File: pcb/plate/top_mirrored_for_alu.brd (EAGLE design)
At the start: 109 x 96 mm, 27 parts

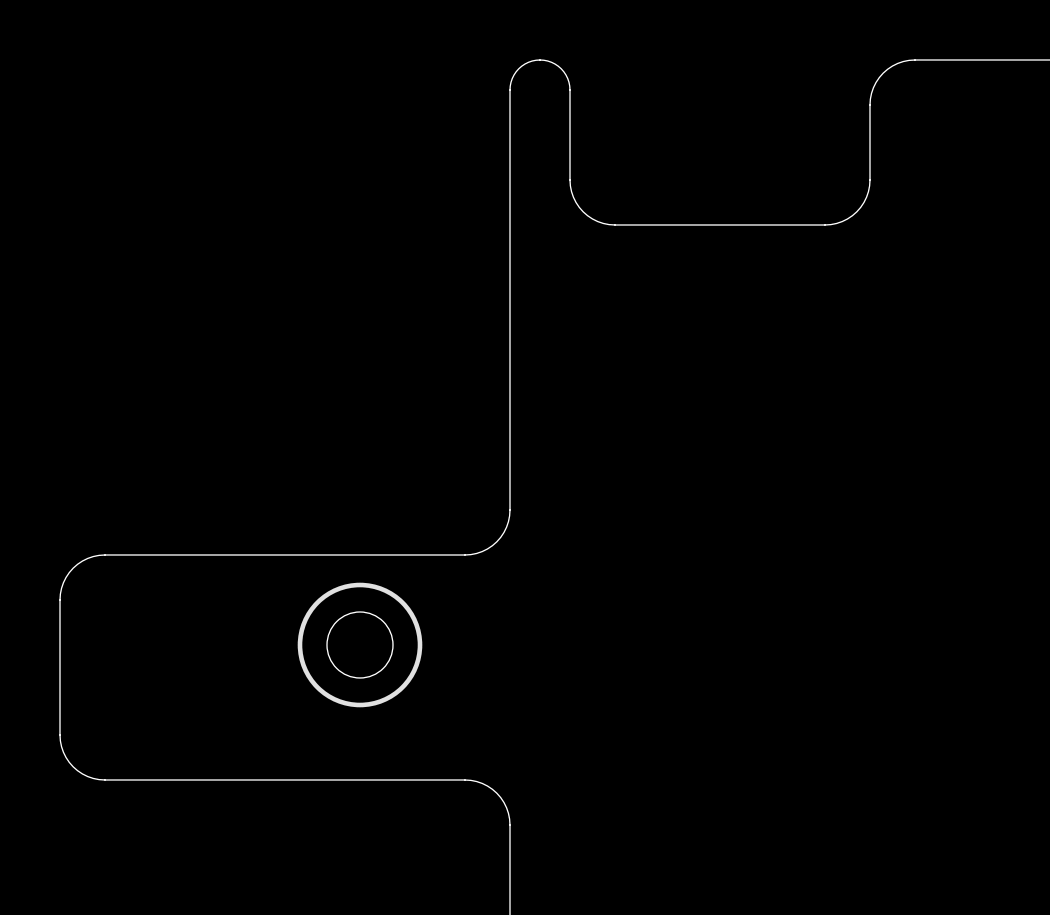
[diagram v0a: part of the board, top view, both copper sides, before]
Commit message: adjusted top plate cutout, removed unused screw hole
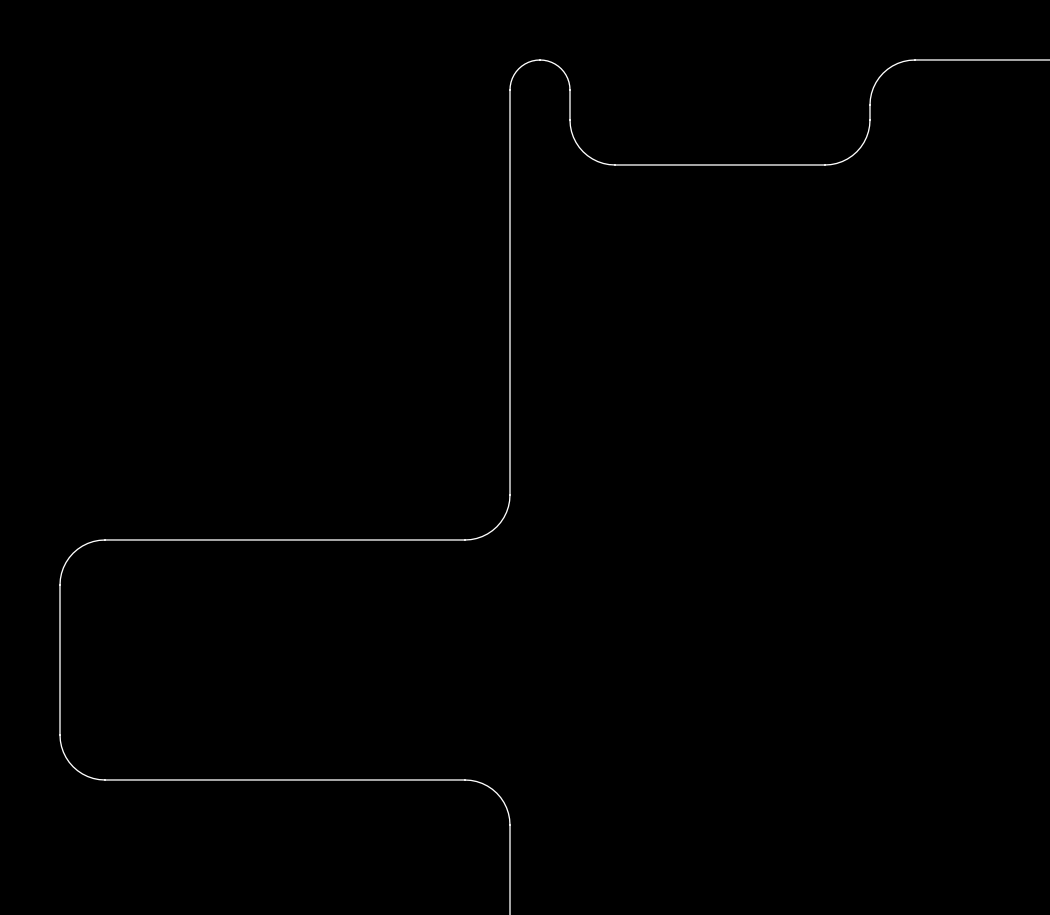
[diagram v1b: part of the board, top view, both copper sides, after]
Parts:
- removed U$17: M2_SCREW_DEV, duckypad:M2_SCREW_FOOT
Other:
- outline, holes or cut-outs redrawn
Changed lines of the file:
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@@
 <wire x1="78.5" y1="96" x2="1.5" y2="96" width="0" layer="20"/>
 <wire x1="1.5" y1="96" x2="0" y2="94.5" width="0" layer="20" curve="90"/>
-<wire x1="0" y1="94.5" x2="0" y2="92" width="0" layer="20"/>
-<wire x1="0" y1="92" x2="-1.5" y2="90.5" width="0" layer="20" curve="-90"/>
-<wire x1="-1.5" y1="90.5" x2="-8.5" y2="90.5" width="0" layer="20"/>
-<wire x1="-8.5" y1="90.5" x2="-10" y2="92" width="0" layer="20" curve="-90"/>
-<wire x1="-10" y1="92" x2="-10" y2="95" width="0" layer="20"/>
+<wire x1="0" y1="94.5" x2="0" y2="94" width="0" layer="20"/>
+<wire x1="0" y1="94" x2="-1.5" y2="92.5" width="0" layer="20" curve="-90"/>
+<wire x1="-1.5" y1="92.5" x2="-8.5" y2="92.5" width="0" layer="20"/>
+<wire x1="-8.5" y1="92.5" x2="-10" y2="94" width="0" layer="20" curve="-90"/>
+<wire x1="-10" y1="94" x2="-10" y2="95" width="0" layer="20"/>
 <wire x1="9.5" y1="0" x2="78.5" y2="0" width="0" layer="20"/>
 <wire x1="78.5" y1="0" x2="82" y2="3.5" width="0" layer="20" curve="90"/>
@@
 <wire x1="6" y1="53" x2="6" y2="3.5" width="0" layer="20"/>
 <wire x1="6" y1="3.5" x2="9.5" y2="0" width="0" layer="20" curve="90"/>
-<wire x1="-13.5" y1="79.5" x2="-25.5" y2="79.5" width="0" layer="20"/>
-<wire x1="-25.5" y1="79.5" x2="-27" y2="78" width="0" layer="20" curve="90"/>
-<wire x1="-27" y1="78" x2="-27" y2="73.5" width="0" layer="20"/>
+<wire x1="-12" y1="95" x2="-12" y2="81.5" width="0" layer="20"/>
+<wire x1="-12" y1="81.5" x2="-13.5" y2="80" width="0" layer="20" curve="-90"/>
+<wire x1="-13.5" y1="80" x2="-25.5" y2="80" width="0" layer="20"/>
+<wire x1="-25.5" y1="80" x2="-27" y2="78.5" width="0" layer="20" curve="90"/>
+<wire x1="-27" y1="78.5" x2="-27" y2="73.5" width="0" layer="20"/>
 <wire x1="-27" y1="73.5" x2="-25.5" y2="72" width="0" layer="20" curve="90"/>
 <wire x1="-25.5" y1="72" x2="-13.5" y2="72" width="0" layer="20"/>
@@
 <wire x1="-10" y1="95" x2="-11" y2="96" width="0" layer="20" curve="90"/>
 <wire x1="-11" y1="96" x2="-12" y2="95" width="0" layer="20" curve="90"/>
-<wire x1="-12" y1="95" x2="-12" y2="81" width="0" layer="20"/>
-<wire x1="-12" y1="81" x2="-13.5" y2="79.5" width="0" layer="20" curve="-90"/>
 <text x="157" y="50" size="1.778" layer="51">big round corner 3.5mm</text>
 </plain>
@@
 <element name="U$12" library="duckypad" package="M2_SCREW_FOOT" value="M2_SCREW_DEV" x="43.5" y="38.5" smashed="yes" rot="MR0"/>
 <element name="U$13" library="duckypad" package="M2_SCREW_FOOT" value="M2_SCREW_DEV" x="24.5" y="19.5" smashed="yes" rot="MR0"/>
-<element name="U$17" library="duckypad" package="M2_SCREW_FOOT" value="M2_SCREW_DEV" x="-17" y="76.5" smashed="yes" rot="MR0"/>
 <element name="U$14" library="duckypad" package="M2_SCREW_FOOT" value="M2_SCREW_DEV" x="62.5" y="76.5" smashed="yes" rot="MR0"/>
 <element name="U$22" library="duckypad" package="M2_SCREW_FOOT" value="M2_SCREW_DEV" x="62.5" y="19.5" smashed="yes" rot="MR0"/>
